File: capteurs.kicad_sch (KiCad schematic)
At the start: 10 parts, among them U2 WSEN-PDUS

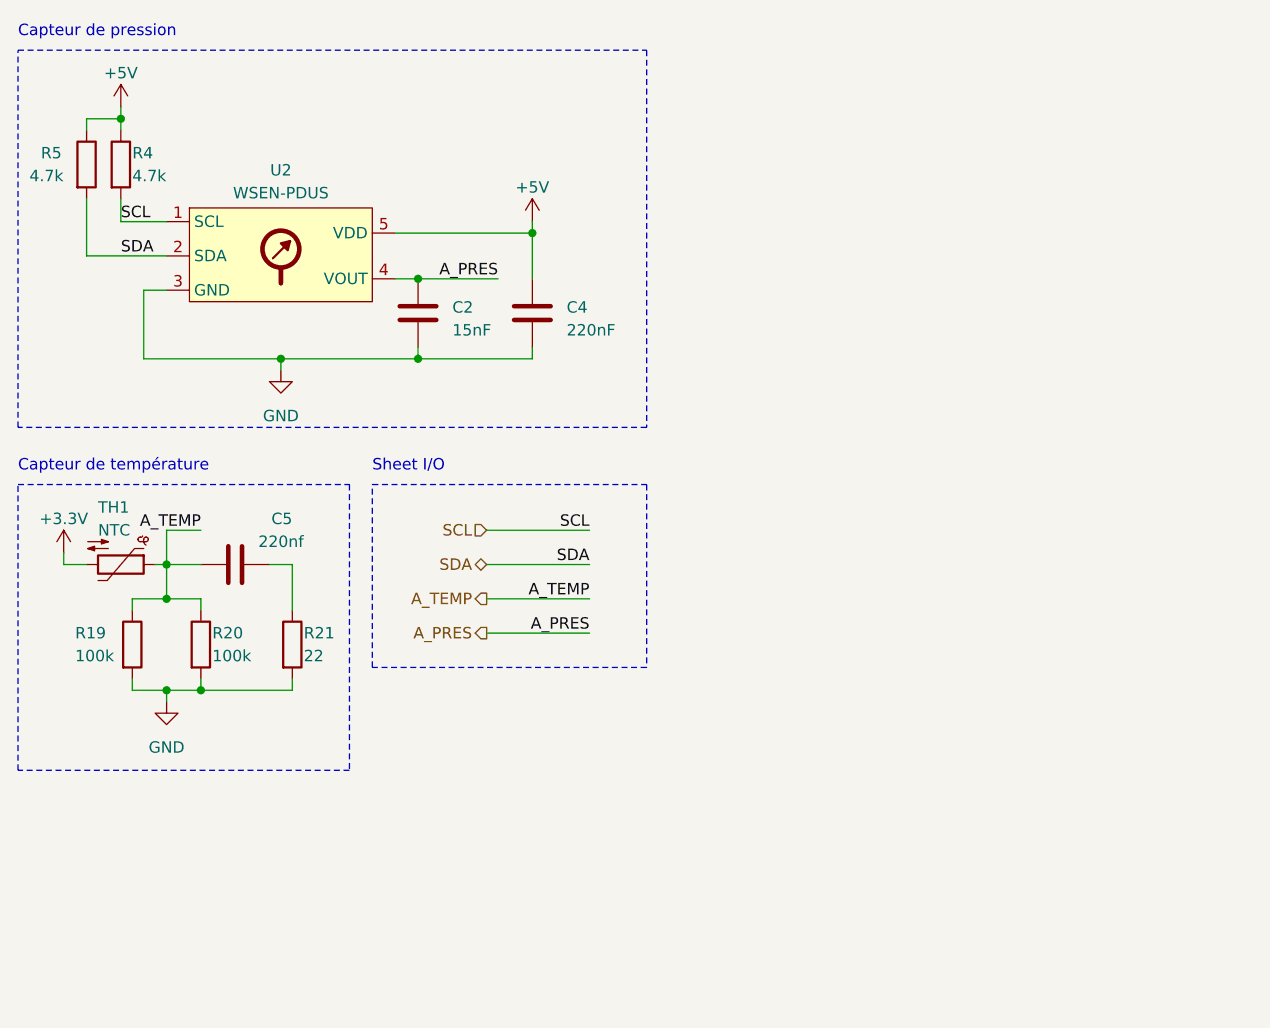
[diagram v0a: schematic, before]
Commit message: Correct CAN interface, add some filtering on sensors + add LCD board power connector
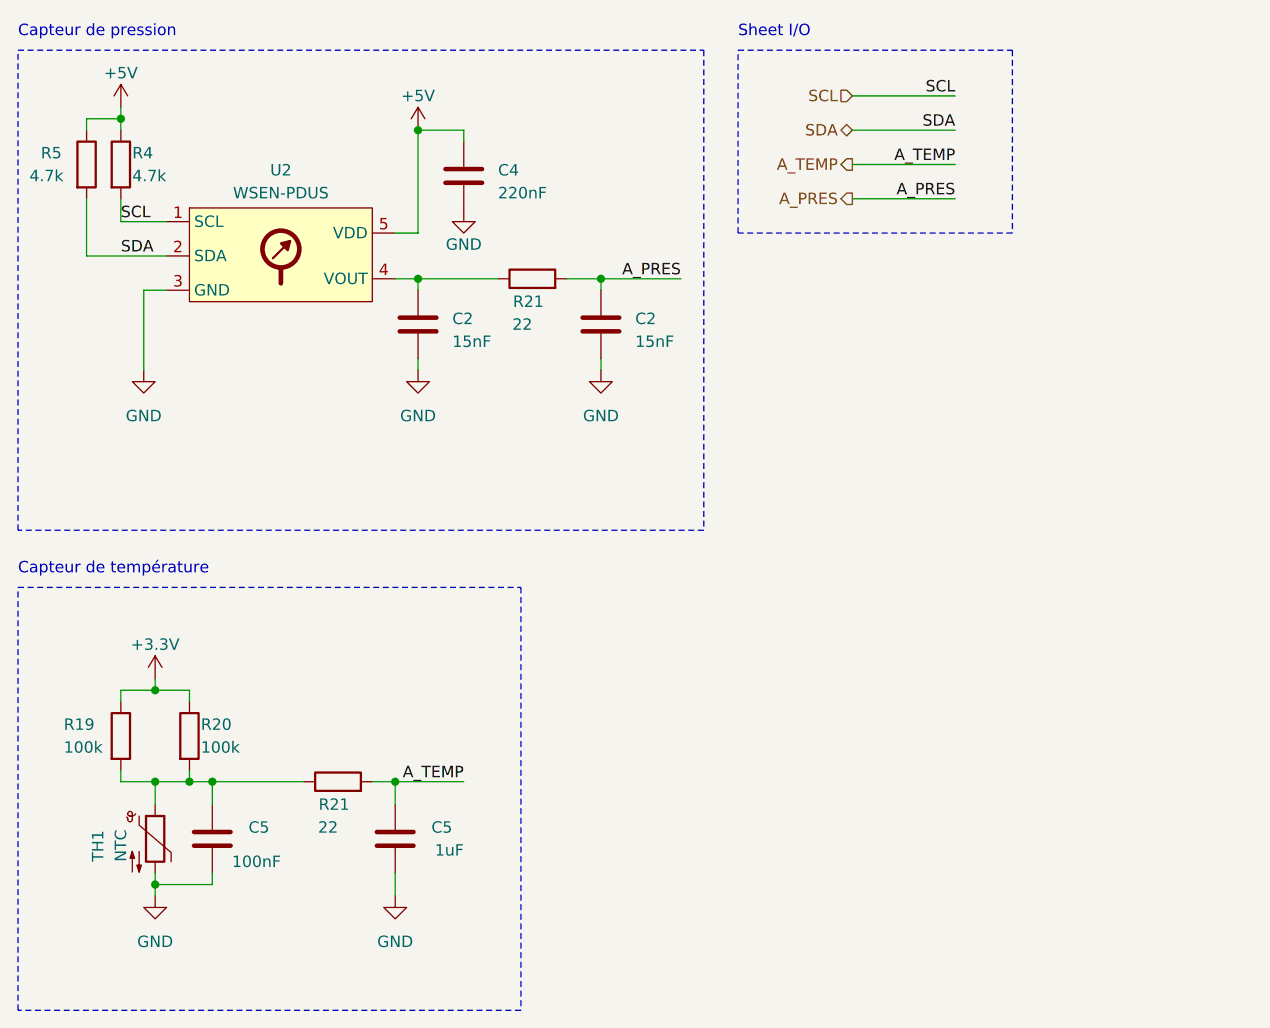
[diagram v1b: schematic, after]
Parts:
- added C2: 15nF, Capacitor_SMD:C_0603_1608Metric, symbol Device:C
- added C5: 100nF, Capacitor_SMD:C_0805_2012Metric, symbol Device:C
- added R21: 22, Resistor_SMD:R_0603_1608Metric, symbol Device:R
- C5: value 220nf -> 1uF
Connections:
- net +3.3V: now also R19.1, R20.1; no longer TH1.2
- net A_PRES: now also C2.1, R21.2; no longer C2.1, U2.4 (VOUT)
- net A_TEMP: now also C5.2, R21.2; no longer C5.1, R19.1, R20.1, TH1.1
- net GND: now also C5.1, TH1.2, C2.2, C5.1; no longer R19.2, R20.2, R21.2
- net at R21.1: now also R19.2, R20.2, TH1.1, C5.2; no longer C5.2
- new net: C2.1, R21.1, U2.4 (VOUT)
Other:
- moved on the sheet: C2, C4, C5, R19, R20, R21, TH1

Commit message: Schematics finished, reanotated sch
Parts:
- C4, C5: footprint Capacitor_SMD:C_0805_2012Metric -> Capacitor_SMD:C_0603_1608Metric

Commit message: Before making power planes
Signal routing done. Added I2C level shifter in schematics.
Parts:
- added C23, C24: 100nF, Capacitor_SMD:C_0603_1608Metric, symbol Device:C_Small
- added R4, R5: 10k, Resistor_SMD:R_0603_1608Metric, symbol Device:R
- added U4: TCA9517DR, Package_SO:SOIC-8_3.9x4.9mm_P1.27mm, symbol ComponentsEvo:TCA9517DR
- R4, R5: value 4.7k -> 10k
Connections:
- net +3.3V: now also C23.1, R4.1, R5.1, U4.1 (VCCA)
- net +5V: now also C24.1, U4.5 (EN), U4.8 (VCCB)
- net GND: now also C23.2, C24.2, U4.4 (GND)
- net SCL: now also R4.2, U4.3 (SDAA); no longer R4.2, U2.1 (SCL)
- net SDA: now also R5.2, U4.2 (SCLA); no longer R5.2, U2.2 (SDA)
- new net SCL_5: R4.2, U2.1 (SCL), U4.7 (SCLB)
- new net SDA_5: R5.2, U2.2 (SDA), U4.6 (SDAB)
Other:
- note added: "Level shifter"
- moved on the sheet: C5, R19, R20, R21, R4, R5, TH1

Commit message: CDR 2025 version WIP
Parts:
- renumbered C4 to C20, C2 to C21, C2 to C22, C5 to C25, C5 to C26, R5 to R25, R4 to R26, R21 to R27, R5 to R28, R4 to R29, R19 to R30, R20 to R31, R21 to R32, U2 to U3
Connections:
- net +5V: no longer C20.1, C24.1, R25.1, R26.1, U3.5 (VDD), U4.8 (VCCB)
- net SCL: now also R28.2, U4.2 (SCLA); no longer R29.2, U4.3 (SDAA)
- net SDA: now also R29.2, U4.3 (SDAA); no longer R28.2, U4.2 (SCLA)
- new net +5VL: C20.1, C24.1, R25.1, R26.1, U3.5 (VDD), U4.8 (VCCB)
